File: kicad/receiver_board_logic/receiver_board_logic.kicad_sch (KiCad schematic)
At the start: 11 parts, among them J2 Motor 1, J3 Motor 2, SW1 On/Off, SW2 Pair/Direction, U4 Dual H Bridge, U5 ESP32-C3-SuperMini

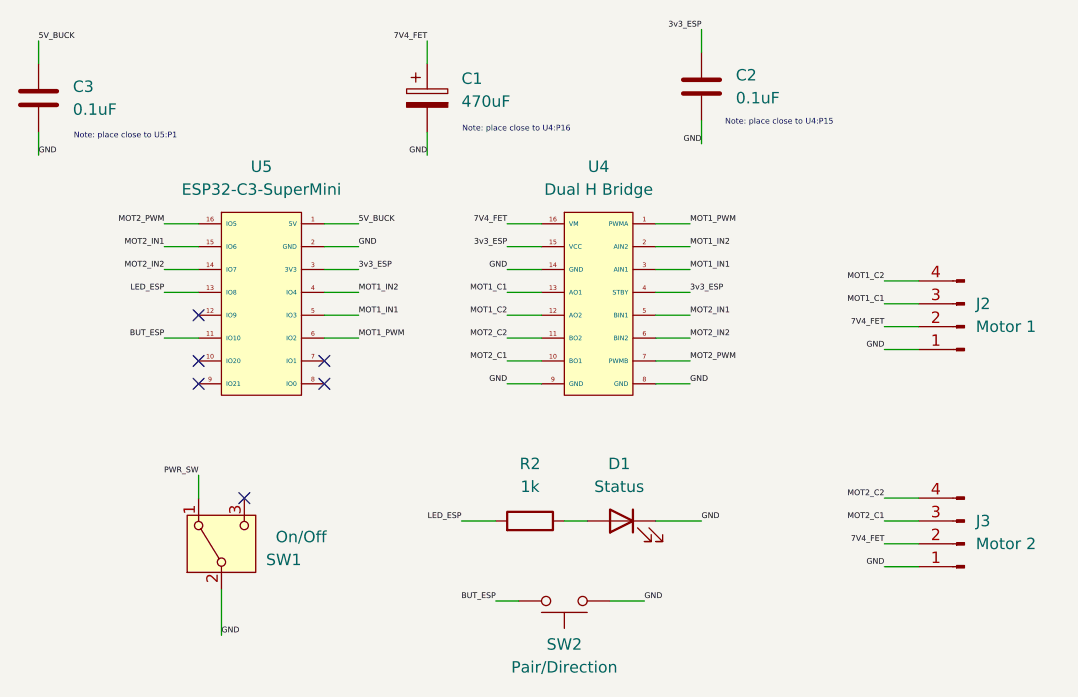
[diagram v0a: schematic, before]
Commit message: Finished generating footprints for all parts. Receiver boards layout and stacking order is still TBD, so renamed them from "uppper" and "lower" to "power" and "logic" as that will likely be the rough distribution of parts between them.
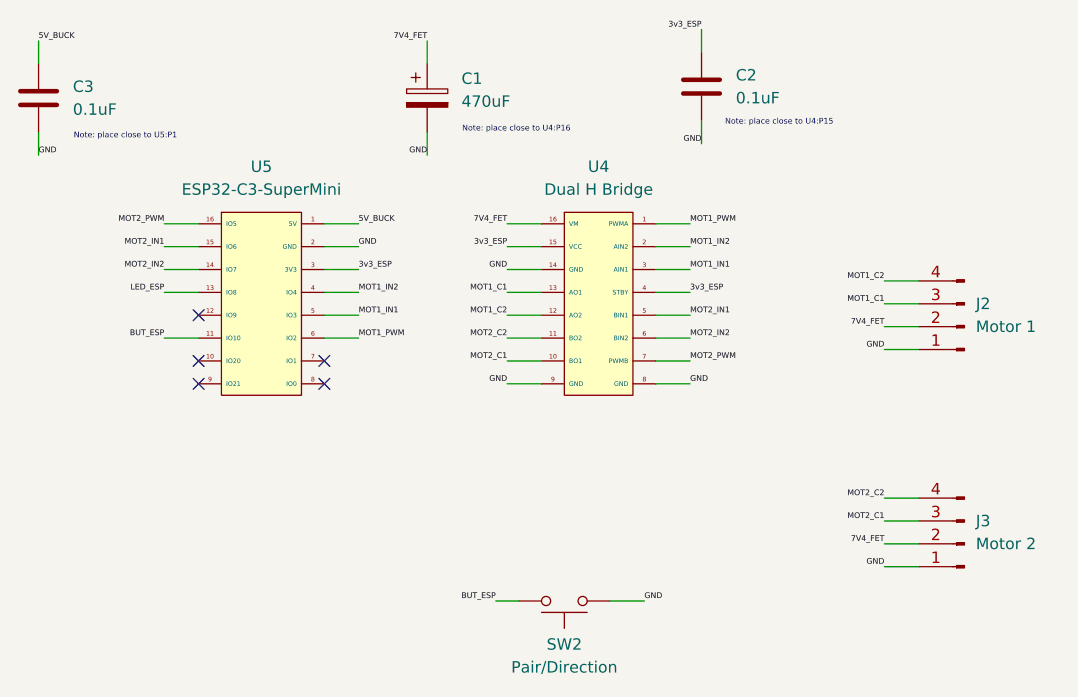
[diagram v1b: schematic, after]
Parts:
- removed D1: Status, LED_THT:LED_D5.0mm, symbol Device:LED
- removed R2: 1k, Resistor_THT:R_Axial_DIN0207_L6.3mm_D2.5mm_P7.62mm_Horizontal, symbol Device:R
- removed SW1: On/Off, ESP32_Lego_PF:Slide_Switch_SPDT_12D00G, symbol Switch:SW_SPDT
- C1: footprint (none) -> Capacitor_THT:CP_Radial_D8.0mm_P5.00mm
- C2, C3: footprint (none) -> Capacitor_THT:C_Disc_D5.0mm_W2.5mm_P5.00mm
- U4: footprint (none) -> ESP32_Lego_PF:TB6612FNG
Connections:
- no-connect marks 6 -> 5
